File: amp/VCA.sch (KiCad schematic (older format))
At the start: 17 parts, among them Q1 DMMT5401, U2 LM13700, U5 TL074

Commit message: update components
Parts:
- C5: footprint KiCad/Capacitors_ThroughHole.pretty:CP_Radial_D4.0mm_P2.00mm -> Capacitor_THT:C_Disc_D3.0mm_W2.0mm_P2.50mm
- Q1: footprint KiCad/kicad-footprints/Package_TO_SOT_SMD.pretty:SOT-23-6 -> Package_TO_SOT_SMD:SOT-23-6
- R21, R22, R23, R24, R25, R26, R27, R28, R29: footprint KiCad/Resistors_ThroughHole.pretty:R_Axial_DIN0204_L3.6mm_D1.6mm_P1.90mm_Vertical -> Resistor_THT:R_Axial_DIN0204_L3.6mm_D1.6mm_P1.90mm_Vertical
- RT1, RT2, RT3: footprint (none) -> Resistor_THT:R_Box_L14.0mm_W5.0mm_P9.00mm
- U2: footprint KiCad/Housings_DIP.pretty:DIP-16_W7.62mm -> Package_DIP:DIP-16_W7.62mm
- U5: footprint KiCad/Housings_DIP.pretty:DIP-14_W7.62mm -> Package_DIP:DIP-14_W7.62mm
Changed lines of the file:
@@
 F 0 "U5" H 4700 4250 50  0000 C CNN
 F 1 "TL074" H 4700 4500 50  0000 C CNN
-F 2 "KiCad/Housings_DIP.pretty:DIP-14_W7.62mm" H 4700 4600 50  0001 C CNN
+F 2 "Package_DIP:DIP-14_W7.62mm" H 4700 4600 50  0001 C CNN
 F 3 "http://www.ti.com/lit/ds/symlink/tl071.pdf" H 4800 4700 50  0001 C CNN
 	2    4750 4500
@@
 F 0 "Q1" H 6500 4650 50  0000 L CNN
 F 1 "DMMT5401" V 6850 4300 50  0000 L CNN
-F 2 "KiCad/kicad-footprints/Package_TO_SOT_SMD.pretty:SOT-23-6" H 6850 4425 50  0001 L CIN
+F 2 "Package_TO_SOT_SMD:SOT-23-6" H 6850 4425 50  0001 L CIN
 F 3 "https://www.diodes.com/assets/Datasheets/ds30437.pdf" H 6650 4500 50  0001 L CNN
 	2    6650 4500
@@
 F 0 "Q1" H 5850 4650 50  0000 L CNN
 F 1 "DMMT5401" V 6250 4300 50  0000 L CNN
-F 2 "KiCad/kicad-footprints/Package_TO_SOT_SMD.pretty:SOT-23-6" H 6200 4425 50  0001 L CIN
+F 2 "Package_TO_SOT_SMD:SOT-23-6" H 6200 4425 50  0001 L CIN
 F 3 "https://www.diodes.com/assets/Datasheets/ds30437.pdf" H 6000 4500 50  0001 L CNN
 	1    6000 4500
@@
 F 0 "R26" V 5180 5550 50  0000 C CNN
 F 1 "22K" V 5100 5550 50  0000 C CNN
-F 2 "KiCad/Resistors_ThroughHole.pretty:R_Axial_DIN0204_L3.6mm_D1.6mm_P1.90mm_Vertical" V 5030 5550 50  0001 C CNN
+F 2 "Resistor_THT:R_Axial_DIN0204_L3.6mm_D1.6mm_P1.90mm_Vertical" V 5030 5550 50  0001 C CNN
 F 3 "" H 5100 5550 50  0001 C CNN
 	1    5100 5550
@@
 F 0 "R28" V 6630 5050 50  0000 C CNN
 F 1 "5K" V 6550 5050 50  0000 C CNN
-F 2 "KiCad/Resistors_ThroughHole.pretty:R_Axial_DIN0204_L3.6mm_D1.6mm_P1.90mm_Vertical" V 6480 5050 50  0001 C CNN
+F 2 "Resistor_THT:R_Axial_DIN0204_L3.6mm_D1.6mm_P1.90mm_Vertical" V 6480 5050 50  0001 C CNN
 F 3 "" H 6550 5050 50  0001 C CNN
 	1    6550 5050
@@
 F 0 "C5" H 5875 5100 50  0000 L CNN
 F 1 "30p" H 5875 4900 50  0000 L CNN
-F 2 "KiCad/Capacitors_ThroughHole.pretty:CP_Radial_D4.0mm_P2.00mm" H 5888 4850 50  0001 C CNN
+F 2 "Capacitor_THT:C_Disc_D3.0mm_W2.0mm_P2.50mm" H 5888 4850 50  0001 C CNN
 F 3 "" H 5850 5000 50  0001 C CNN
 	1    5850 5000
@@
 F 0 "R25" V 4830 3950 50  0000 C CNN
 F 1 "3K3" V 4750 3950 50  0000 C CNN
-F 2 "KiCad/Resistors_ThroughHole.pretty:R_Axial_DIN0204_L3.6mm_D1.6mm_P1.90mm_Vertical" V 4680 3950 50  0001 C CNN
+F 2 "Resistor_THT:R_Axial_DIN0204_L3.6mm_D1.6mm_P1.90mm_Vertical" V 4680 3950 50  0001 C CNN
 F 3 "" H 4750 3950 50  0001 C CNN
 	1    4750 3950
@@
 F 0 "R22" V 4080 3950 50  0000 C CNN
 F 1 "120K" V 4000 3950 50  0000 C CNN
-F 2 "KiCad/Resistors_ThroughHole.pretty:R_Axial_DIN0204_L3.6mm_D1.6mm_P1.90mm_Vertical" V 3930 3950 50  0001 C CNN
+F 2 "Resistor_THT:R_Axial_DIN0204_L3.6mm_D1.6mm_P1.90mm_Vertical" V 3930 3950 50  0001 C CNN
 F 3 "" H 4000 3950 50  0001 C CNN
 	1    4000 3950
@@
 F 0 "R23" V 4080 4400 50  0000 C CNN
 F 1 "270K" V 4000 4400 50  0000 C CNN
-F 2 "KiCad/Resistors_ThroughHole.pretty:R_Axial_DIN0204_L3.6mm_D1.6mm_P1.90mm_Vertical" V 3930 4400 50  0001 C CNN
+F 2 "Resistor_THT:R_Axial_DIN0204_L3.6mm_D1.6mm_P1.90mm_Vertical" V 3930 4400 50  0001 C CNN
 F 3 "" H 4000 4400 50  0001 C CNN
 	1    4000 4400
@@
 F 0 "R24" V 4280 2200 50  0000 C CNN
 F 1 "3K3" V 4200 2200 50  0000 C CNN
-F 2 "KiCad/Resistors_ThroughHole.pretty:R_Axial_DIN0204_L3.6mm_D1.6mm_P1.90mm_Vertical" V 4130 2200 50  0001 C CNN
+F 2 "Resistor_THT:R_Axial_DIN0204_L3.6mm_D1.6mm_P1.90mm_Vertical" V 4130 2200 50  0001 C CNN
 F 3 "" H 4200 2200 50  0001 C CNN
 	1    4200 2200
@@
 F 0 "U5" H 5900 5550 50  0000 C CNN
 F 1 "TL074" H 5750 5400 50  0000 C CNN
-F 2 "KiCad/Housings_DIP.pretty:DIP-14_W7.62mm" H 5750 5500 50  0001 C CNN
+F 2 "Package_DIP:DIP-14_W7.62mm" H 5750 5500 50  0001 C CNN
 F 3 "http://www.ti.com/lit/ds/symlink/tl071.pdf" H 5850 5600 50  0001 C CNN
 	3    5800 5400
@@
 F 0 "R27" V 6350 2600 50  0000 C CNN
 F 1 "27K" V 6450 2600 50  0000 C CNN
-F 2 "KiCad/Resistors_ThroughHole.pretty:R_Axial_DIN0204_L3.6mm_D1.6mm_P1.90mm_Vertical" V 6380 2600 50  0001 C CNN
+F 2 "Resistor_THT:R_Axial_DIN0204_L3.6mm_D1.6mm_P1.90mm_Vertical" V 6380 2600 50  0001 C CNN
 F 3 "~" H 6450 2600 50  0001 C CNN
 	1    6450 2600
@@
 F 0 "U5" H 7200 2550 50  0000 C CNN
 F 1 "TL074" H 7100 2700 50  0000 C CNN
-F 2 "KiCad/Housings_DIP.pretty:DIP-14_W7.62mm" H 7100 2800 50  0001 C CNN
+F 2 "Package_DIP:DIP-14_W7.62mm" H 7100 2800 50  0001 C CNN
 F 3 "http://www.ti.com/lit/ds/symlink/tl071.pdf" H 7200 2900 50  0001 C CNN
 	4    7150 2700
@@
 F 0 "R29" V 6900 2400 50  0000 C CNN
 F 1 "22K" V 7000 2400 50  0000 C CNN
-F 2 "KiCad/Resistors_ThroughHole.pretty:R_Axial_DIN0204_L3.6mm_D1.6mm_P1.90mm_Vertical" V 6930 2400 50  0001 C CNN
+F 2 "Resistor_THT:R_Axial_DIN0204_L3.6mm_D1.6mm_P1.90mm_Vertical" V 6930 2400 50  0001 C CNN
 F 3 "~" H 7000 2400 50  0001 C CNN
 	1    7000 2400
@@
 F 0 "U5" H 10858 1196 50  0000 L CNN
 F 1 "TL074" H 10858 1105 50  0000 L CNN
-F 2 "KiCad/Housings_DIP.pretty:DIP-14_W7.62mm" H 10850 1250 50  0001 C CNN
+F 2 "Package_DIP:DIP-14_W7.62mm" H 10850 1250 50  0001 C CNN
 F 3 "http://www.ti.com/lit/ds/symlink/tl071.pdf" H 10950 1350 50  0001 C CNN
 	5    10900 1150
@@
 F 0 "U2" H 5650 2967 50  0000 C CNN
 F 1 "LM13700" H 5650 2876 50  0000 C CNN
-F 2 "KiCad/Housings_DIP.pretty:DIP-16_W7.62mm" H 5350 2625 50  0001 C CNN
+F 2 "Package_DIP:DIP-16_W7.62mm" H 5350 2625 50  0001 C CNN
 F 3 "http://www.ti.com/lit/ds/symlink/lm13700.pdf" H 5350 2625 50  0001 C CNN
 	1    5650 2600
@@
 F 0 "R21" V 3630 2600 50  0000 C CNN
 F 1 "820K" V 3550 2600 50  0000 C CNN
-F 2 "KiCad/Resistors_ThroughHole.pretty:R_Axial_DIN0204_L3.6mm_D1.6mm_P1.90mm_Vertical" V 3480 2600 50  0001 C CNN
+F 2 "Resistor_THT:R_Axial_DIN0204_L3.6mm_D1.6mm_P1.90mm_Vertical" V 3480 2600 50  0001 C CNN
 F 3 "" H 3550 2600 50  0001 C CNN
 	1    3550 2600
@@
 F 0 "RT2" H 5200 6000 50  0000 L CNN
 F 1 "5K" H 5200 5900 50  0000 L CNN
-F 2 "" V 5030 5950 50  0001 C CNN
+F 2 "Resistor_THT:R_Box_L14.0mm_W5.0mm_P9.00mm" V 5030 5950 50  0001 C CNN
 F 3 "~" H 5100 5950 50  0001 C CNN
 	1    5100 5950
@@
 F 0 "U5" H 4250 2500 50  0000 C CNN
 F 1 "TL074" H 4150 2700 50  0000 C CNN
-F 2 "KiCad/Housings_DIP.pretty:DIP-14_W7.62mm" H 4150 2800 50  0001 C CNN
+F 2 "Package_DIP:DIP-14_W7.62mm" H 4150 2800 50  0001 C CNN
 F 3 "http://www.ti.com/lit/ds/symlink/tl071.pdf" H 4250 2900 50  0001 C CNN
 	1    4200 2700
@@
 F 0 "RT1" V 3360 4400 50  0000 C CNN
 F 1 "50K" V 3451 4400 50  0000 C CNN
-F 2 "" V 3530 4400 50  0001 C CNN
+F 2 "Resistor_THT:R_Box_L14.0mm_W5.0mm_P9.00mm" V 3530 4400 50  0001 C CNN
 F 3 "~" H 3600 4400 50  0001 C CNN
 	1    3600 4400
@@
 F 0 "RT3" V 7615 2400 50  0000 C CNN
 F 1 "10K" V 7524 2400 50  0000 C CNN
-F 2 "" V 7280 2400 50  0001 C CNN
+F 2 "Resistor_THT:R_Box_L14.0mm_W5.0mm_P9.00mm" V 7280 2400 50  0001 C CNN
 F 3 "~" H 7350 2400 50  0001 C CNN
 	1    7350 2400

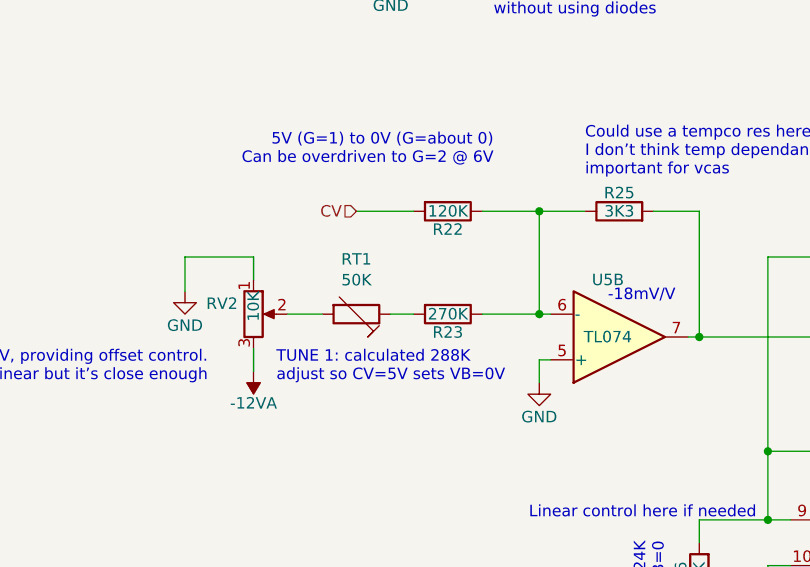
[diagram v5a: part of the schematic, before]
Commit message: adjusted amp to a 10V control voltage range
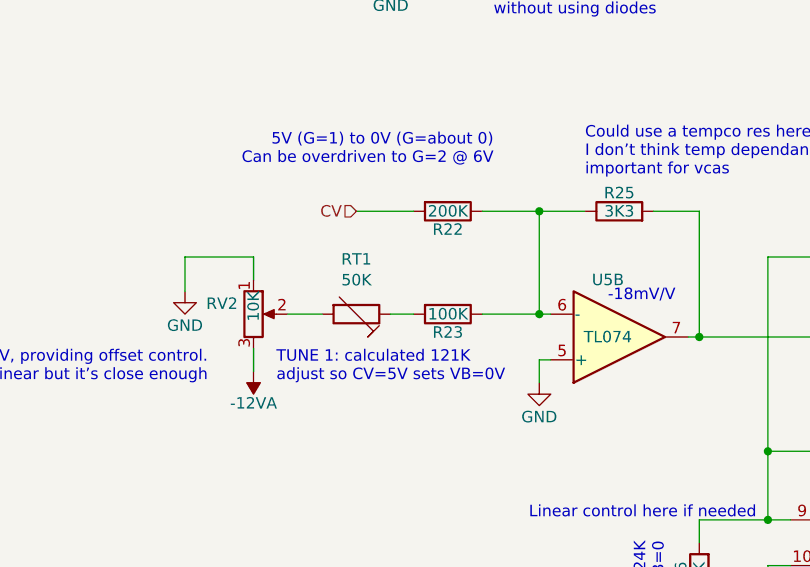
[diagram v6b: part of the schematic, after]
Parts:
- R22: value 120K -> 200K
- R23: value 270K -> 100K
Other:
- note added: "TUNE 1: calculated 121K\nadjust so CV=5V sets VB=0V"
- note removed: "TUNE 1: calculated 288K\nadjust so CV=5V sets VB=0V"
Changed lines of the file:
@@
 AR Path="/5EE9163B/5EBBC2D7" Ref="R40"  Part="1"
 F 0 "R22" V 4080 3950 50  0000 C CNN
-F 1 "120K" V 4000 3950 50  0000 C CNN
+F 1 "200K" V 4000 3950 50  0000 C CNN
 F 2 "Resistor_THT:R_Axial_DIN0204_L3.6mm_D1.6mm_P1.90mm_Vertical" V 3930 3950 50  0001 C CNN
 F 3 "" H 4000 3950 50  0001 C CNN
@@
 AR Path="/5EE9163B/5EBBC2E3" Ref="R41"  Part="1"
 F 0 "R23" V 4080 4400 50  0000 C CNN
-F 1 "270K" V 4000 4400 50  0000 C CNN
+F 1 "100K" V 4000 4400 50  0000 C CNN
 F 2 "Resistor_THT:R_Axial_DIN0204_L3.6mm_D1.6mm_P1.90mm_Vertical" V 3930 4400 50  0001 C CNN
 F 3 "" H 4000 4400 50  0001 C CNN
@@
 	3200 2600 3400 2600
 Text Notes 3250 4700 0    50   ~ 0
-TUNE 1: calculated 288K\nadjust so CV=5V sets VB=0V
+TUNE 1: calculated 121K\nadjust so CV=5V sets VB=0V
 Text Notes 7650 2400 0    50   ~ 0
 TUNE 3: calculated 27K\nadjust to 5V at g=1

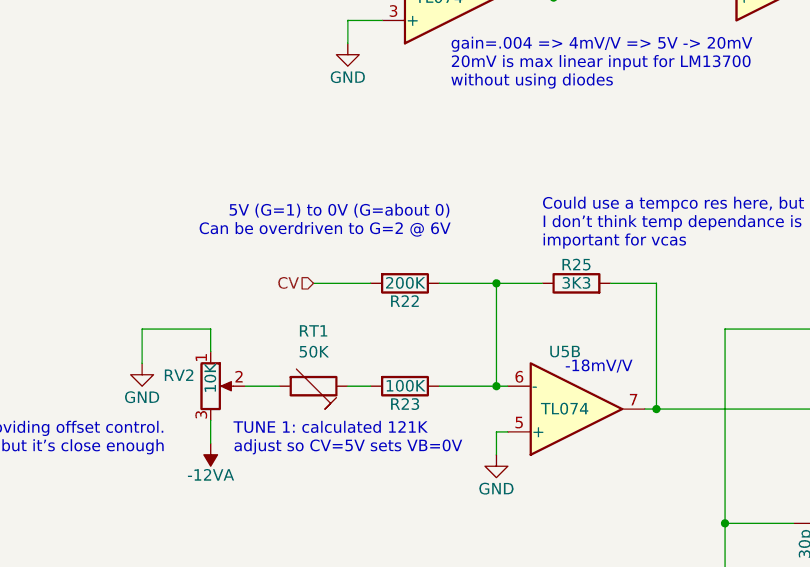
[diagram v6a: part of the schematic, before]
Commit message: corrections based on prototype pcb
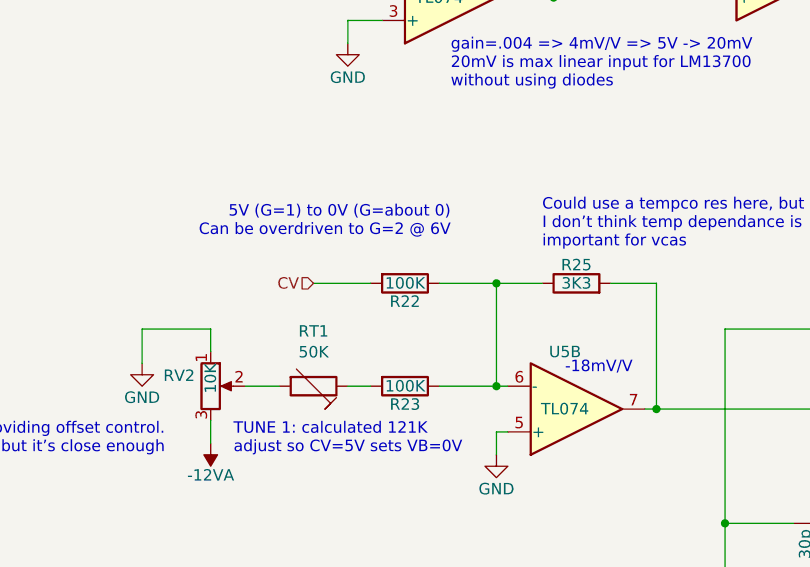
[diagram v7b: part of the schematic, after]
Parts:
- R22: value 200K -> 100K
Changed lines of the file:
@@
 AR Path="/5EE9163B/5EBBC2D7" Ref="R40"  Part="1"
 F 0 "R22" V 4080 3950 50  0000 C CNN
-F 1 "200K" V 4000 3950 50  0000 C CNN
+F 1 "100K" V 4000 3950 50  0000 C CNN
 F 2 "Resistor_THT:R_Axial_DIN0204_L3.6mm_D1.6mm_P1.90mm_Vertical" V 3930 3950 50  0001 C CNN
 F 3 "" H 4000 3950 50  0001 C CNN
